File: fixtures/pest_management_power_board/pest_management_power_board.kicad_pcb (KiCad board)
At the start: 2 copper layers, 105 x 65 mm, 9 parts, among them J2 SEALED_COMMERCIAL_HV_MODULE_I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, J3 HV_POS_GRID, J4 HV_NEG_GRID, SW1 MOMENTARY_NO_10A_DC_PATH

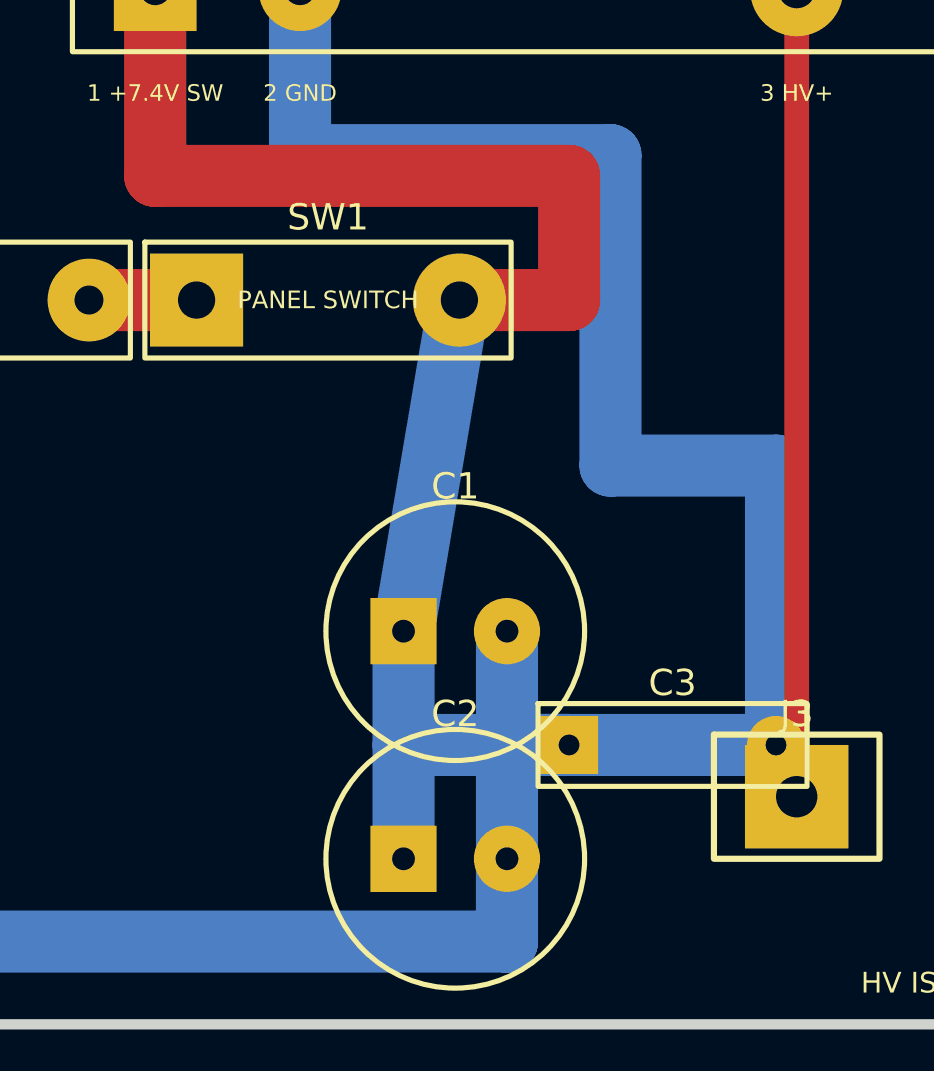
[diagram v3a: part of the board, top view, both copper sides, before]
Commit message: Correct Rev B LV to HV clearance geometry
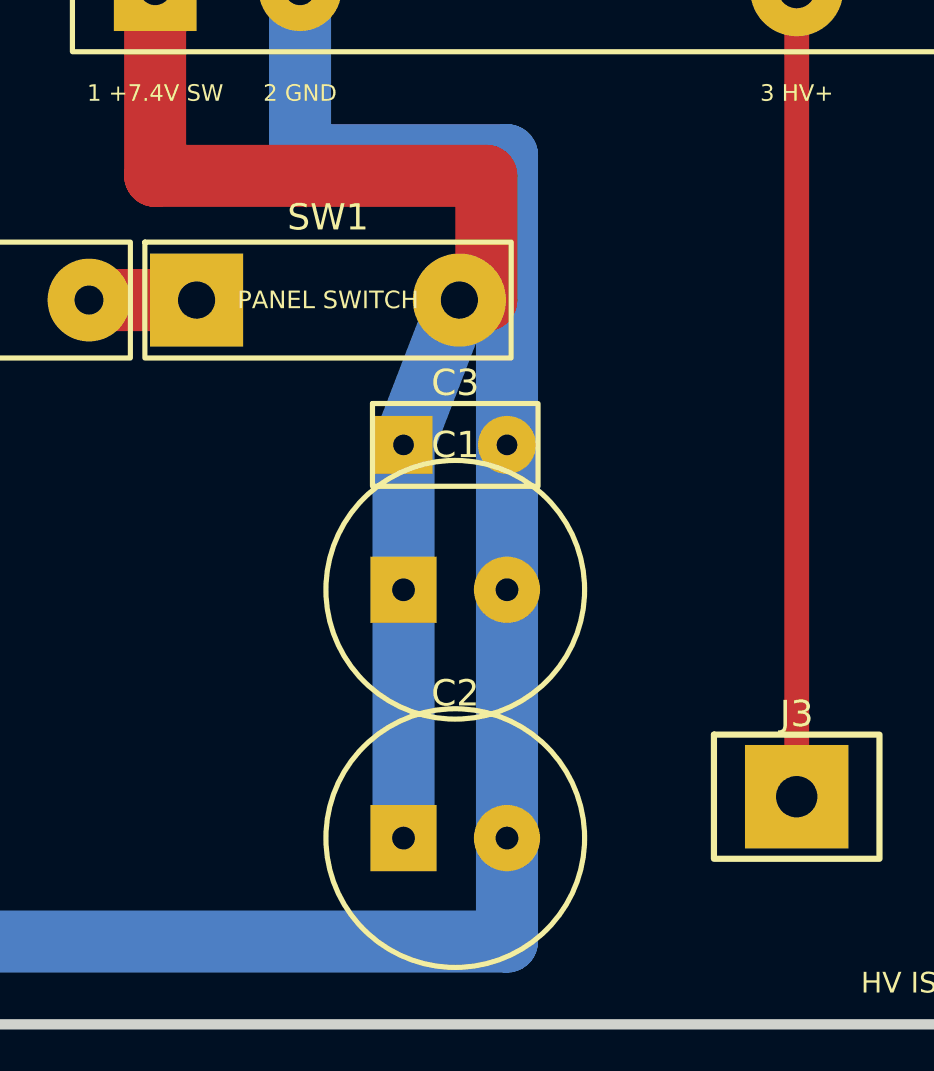
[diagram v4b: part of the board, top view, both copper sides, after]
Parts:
- C3: footprint Custom:FILM_CAP_P10 -> Custom:FILM_CAP_P5
- moved C3 16.6 mm to (74.0, 57.0)
- moved C1 2.00 mm to (74.0, 64.0)
- moved C2 1.00 mm to (74.0, 76.0)
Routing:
- net GND: track 168.4 -> 132.9 mm
- net +7V4_SW: track 75.5 -> 58.8 mm
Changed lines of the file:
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@@
     (pad "2" thru_hole circle (at 12.7 0) (size 4.5 4.5) (drill 1.8) (layers "*.Cu" "*.Mask") (net 3 "+7V4_SW"))
   )
-  (footprint "Custom:CP_RADIAL_12P5MM_P5" (layer "F.Cu") (at 74 66)
+  (footprint "Custom:CP_RADIAL_12P5MM_P5" (layer "F.Cu") (at 74 64)
     (property "Reference" "C1" (at 2.5 -7 0) (layer "F.SilkS"))
     (property "Value" "2200uF_16V_LOW_ESR" (at 2.5 7 0) (layer "F.Fab") hide)
@@
     (pad "2" thru_hole circle (at 5 0) (size 3.2 3.2) (drill 1.1) (layers "*.Cu" "*.Mask") (net 4 "GND"))
   )
-  (footprint "Custom:CP_RADIAL_12P5MM_P5" (layer "F.Cu") (at 74 77)
+  (footprint "Custom:CP_RADIAL_12P5MM_P5" (layer "F.Cu") (at 74 76)
     (property "Reference" "C2" (at 2.5 -7 0) (layer "F.SilkS"))
     (property "Value" "2200uF_16V_LOW_ESR" (at 2.5 7 0) (layer "F.Fab") hide)
@@
     (pad "2" thru_hole circle (at 5 0) (size 3.2 3.2) (drill 1.1) (layers "*.Cu" "*.Mask") (net 4 "GND"))
   )
-  (footprint "Custom:FILM_CAP_P10" (layer "F.Cu") (at 82 71.5)
-    (property "Reference" "C3" (at 5 -3 0) (layer "F.SilkS"))
-    (property "Value" "1uF_25V_FILM" (at 5 3 0) (layer "F.Fab") hide)
-    (fp_rect (start -1.5 -2) (end 11.5 2) (stroke (width 0.25) (type default)) (fill none) (layer "F.SilkS"))
+  (footprint "Custom:FILM_CAP_P5" (layer "F.Cu") (at 74 57)
+    (property "Reference" "C3" (at 2.5 -3 0) (layer "F.SilkS"))
+    (property "Value" "1uF_25V_FILM" (at 2.5 3 0) (layer "F.Fab") hide)
+    (fp_rect (start -1.5 -2) (end 6.5 2) (stroke (width 0.25) (type default)) (fill none) (layer "F.SilkS"))
     (pad "1" thru_hole rect (at 0 0) (size 2.8 2.8) (drill 1.0) (layers "*.Cu" "*.Mask") (net 3 "+7V4_SW"))
-    (pad "2" thru_hole circle (at 10 0) (size 2.8 2.8) (drill 1.0) (layers "*.Cu" "*.Mask") (net 4 "GND"))
+    (pad "2" thru_hole circle (at 5 0) (size 2.8 2.8) (drill 1.0) (layers "*.Cu" "*.Mask") (net 4 "GND"))
   )
   (footprint "Custom:HV_MODULE_4PIN_ISOLATED" (layer "F.Cu") (at 0 0)
@@
   (segment (start 28 50) (end 41 50) (width 3.0) (layer "F.Cu") (net 1))
   (segment (start 58.8 50) (end 64 50) (width 3.0) (layer "F.Cu") (net 2))
-  (segment (start 76.7 50) (end 82 50) (width 3.0) (layer "F.Cu") (net 3))
-  (segment (start 82 50) (end 82 44) (width 3.0) (layer "F.Cu") (net 3))
-  (segment (start 82 44) (end 62 44) (width 3.0) (layer "F.Cu") (net 3))
+  (segment (start 76.7 50) (end 78 50) (width 3.0) (layer "F.Cu") (net 3))
+  (segment (start 78 50) (end 78 44) (width 3.0) (layer "F.Cu") (net 3))
+  (segment (start 78 44) (end 62 44) (width 3.0) (layer "F.Cu") (net 3))
   (segment (start 62 44) (end 62 35) (width 3.0) (layer "F.Cu") (net 3))
-  (segment (start 76.7 50) (end 74 66) (width 3.0) (layer "B.Cu") (net 3))
-  (segment (start 74 66) (end 74 77) (width 3.0) (layer "B.Cu") (net 3))
-  (segment (start 74 71.5) (end 82 71.5) (width 3.0) (layer "B.Cu") (net 3))
+  (segment (start 76.7 50) (end 74 57) (width 3.0) (layer "B.Cu") (net 3))
+  (segment (start 74 57) (end 74 76) (width 3.0) (layer "B.Cu") (net 3))
   (segment (start 33.08 50) (end 33.08 81) (width 3.0) (layer "B.Cu") (net 4))
   (segment (start 33.08 81) (end 79 81) (width 3.0) (layer "B.Cu") (net 4))
-  (segment (start 79 81) (end 79 66) (width 3.0) (layer "B.Cu") (net 4))
-  (segment (start 79 77) (end 79 81) (width 3.0) (layer "B.Cu") (net 4))
-  (segment (start 79 71.5) (end 92 71.5) (width 3.0) (layer "B.Cu") (net 4))
-  (segment (start 92 71.5) (end 92 58) (width 3.0) (layer "B.Cu") (net 4))
-  (segment (start 92 58) (end 84 58) (width 3.0) (layer "B.Cu") (net 4))
-  (segment (start 84 58) (end 84 43) (width 3.0) (layer "B.Cu") (net 4))
-  (segment (start 84 43) (end 69 43) (width 3.0) (layer "B.Cu") (net 4))
+  (segment (start 79 81) (end 79 57) (width 3.0) (layer "B.Cu") (net 4))
+  (segment (start 79 57) (end 79 43) (width 3.0) (layer "B.Cu") (net 4))
+  (segment (start 79 43) (end 69 43) (width 3.0) (layer "B.Cu") (net 4))
   (segment (start 69 43) (end 69 35) (width 3.0) (layer "B.Cu") (net 4))
   (segment (start 93 35) (end 93 74) (width 1.2) (layer "F.Cu") (net 5))
